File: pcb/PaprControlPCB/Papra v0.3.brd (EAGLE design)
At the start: 30 x 45 mm, 32 parts, among them Q1 AO3400A (C20917), U1 LP2985-50DBVR (C74511), U2 ATTINYX04SOIC14

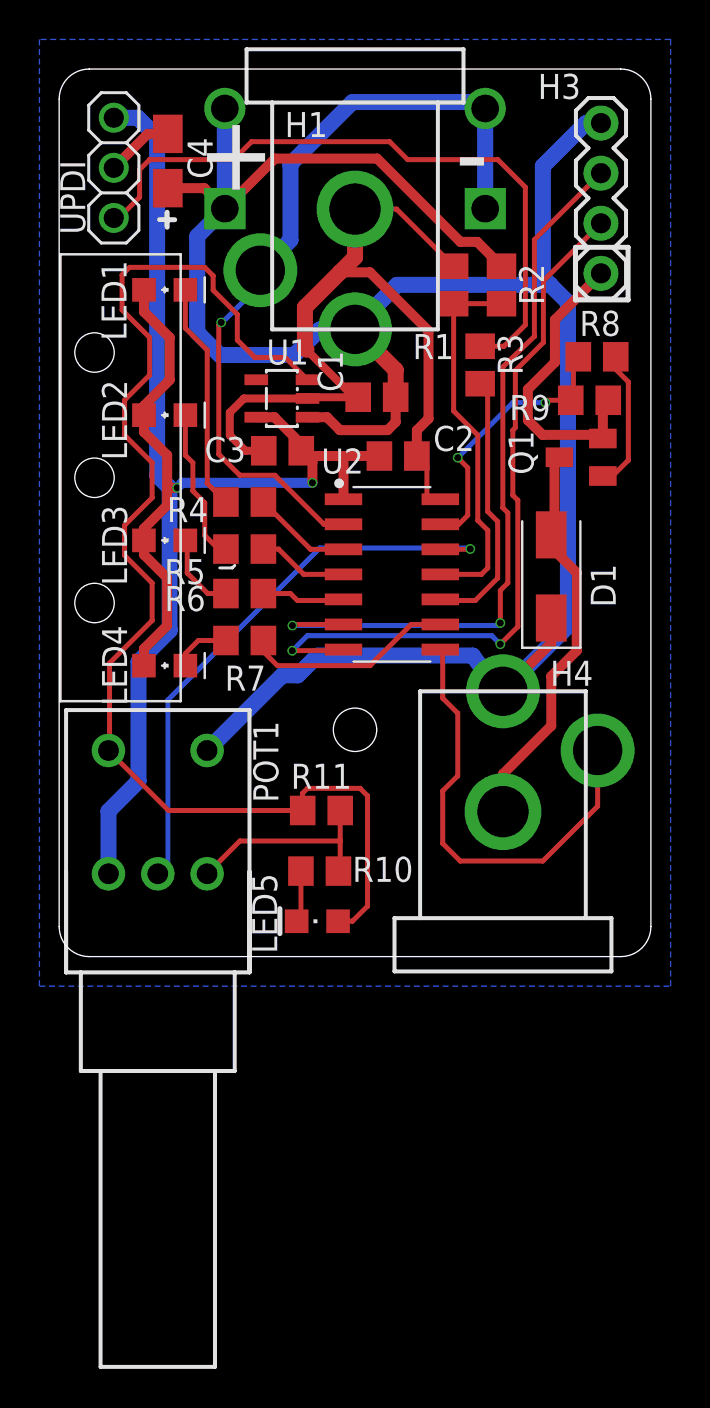
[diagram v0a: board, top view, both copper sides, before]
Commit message: Added 1A resettable fuse to 12V power
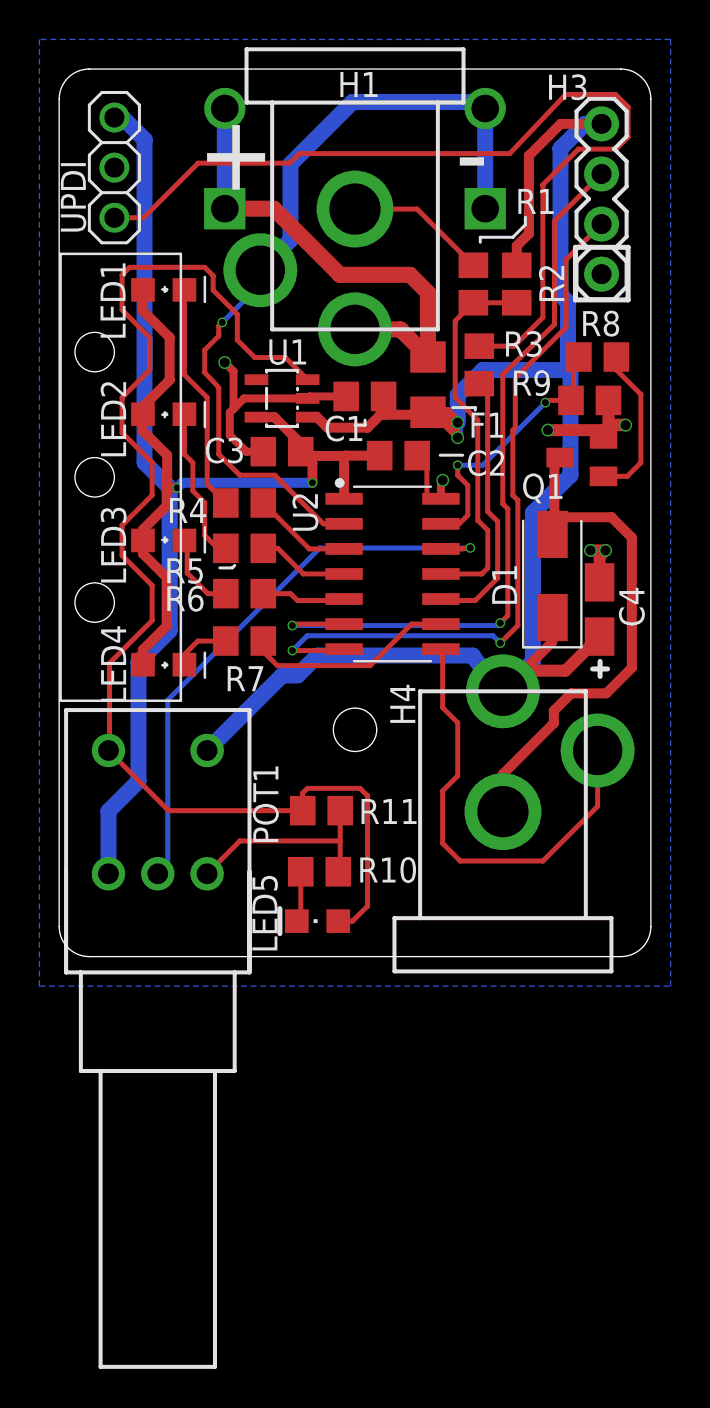
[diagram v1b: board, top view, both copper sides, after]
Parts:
- added F1: 13.2V 1.8A (C70081), SparkFun-Fuses:1206
- moved C4 31.6 mm to (12.4, -4.90)
- moved R1 1.00 mm to (6.00, 11.6)
- moved R2 0.77 mm to (8.20, 11.6)
- moved C1 0.61 mm to (0.50, 5.90)
- moved LED2 0.07 mm to (-9.70, 5.00)
- moved LED4 0.07 mm to (-9.70, -7.70)
- moved D1 0.06 mm to (10.0, -3.20)
- moved C3 0.05 mm to (-3.70, 3.10)
- moved H3 0.05 mm to (12.5, 12.1)
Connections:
- new net 12V-F: BATT+.1, BATT+.2, F1.1, H1.PWR
- net +12V: now also F1.2; no longer BATT+.1, BATT+.2, H1.PWR
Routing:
- net GND: track 72.4 -> 43.4 mm, vias 0 -> 6
- net +12V: track 117.9 -> 91.2 mm, vias 0 -> 2
- net 12V-F: track 0.00 -> 24.7 mm
- net UPDI: track 34.0 -> 46.3 mm
- net FAN-GND: track 20.2 -> 27.0 mm
- net FETGATE: track 7.13 -> 8.05 mm
- net GND-SWITCH: track 40.4 -> 41.0 mm
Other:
- board text added: "21JAN2021"
- board text added: "v.2 changelog - BATTERY Tabs swapped (polarity, same position) - SMT Components Moved, won't affect mechanical - D1 package changed (was SMB, is SMA) v.3 changelog - Added mounting hole - Added fuse, moved SMT components to fit - Adjustments for JLC DRU, pad override was 40%, changed to 25% - Silk cleanup"
- board text removed: "18JAN2021"
- board text removed: "v.2 changelog - BATTERY Tabs swapped (polarity, same position) - SMT Components Moved, won't affect mechanical - D1 package changed (was SMB, is SMA) v.3 changelog - Added mounting hole - Adjustments for JLC DRU, pad override was 40%, changed to 25% - Silk cleanup"

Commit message: v0.3 release candidate
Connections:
- net +5V: now also POT1.3; no longer POT1.1
- net FAN-PWM: now also U2.9; no longer U2.13
- net FAN-SENSE: now also U2.13; no longer U2.8
- net GND: now also POT1.1; no longer POT1.3
- net LED4: now also U2.8; no longer U2.9
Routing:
- net FAN-SENSE: track 22.7 -> 34.3 mm
- net +5V: track 82.4 -> 93.0 mm
- net FAN-PWM: track 13.8 -> 21.6 mm
- net GND: track 43.4 -> 47.5 mm
- net LED4: track 10.7 -> 10.2 mm
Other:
- board text added: "05FEB2021"
- board text added: "v.2 changelog - BATTERY Tabs swapped (polarity, same position) - SMT Components Moved, won't affect mechanical - D1 package changed (was SMB, is SMA) v.3 changelog (see schematic for signal changes) - Added mounting hole - Added fuse, moved SMT components to fit - Adjustments for JLC DRU, pad override was 40%, reduced to 25% - Silk cleanup - Changed Battery Tab package to round pads (was square)"
- board text removed: "21JAN2021"
- board text removed: "v.2 changelog - BATTERY Tabs swapped (polarity, same position) - SMT Components Moved, won't affect mechanical - D1 package changed (was SMB, is SMA) v.3 changelog - Added mounting hole - Added fuse, moved SMT components to fit - Adjustments for JLC DRU, pad override was 40%, changed to 25% - Silk cleanup"
